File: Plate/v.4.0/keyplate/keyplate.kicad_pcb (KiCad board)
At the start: 2 copper layers, 285.4 x 94.9 mm, 21 parts

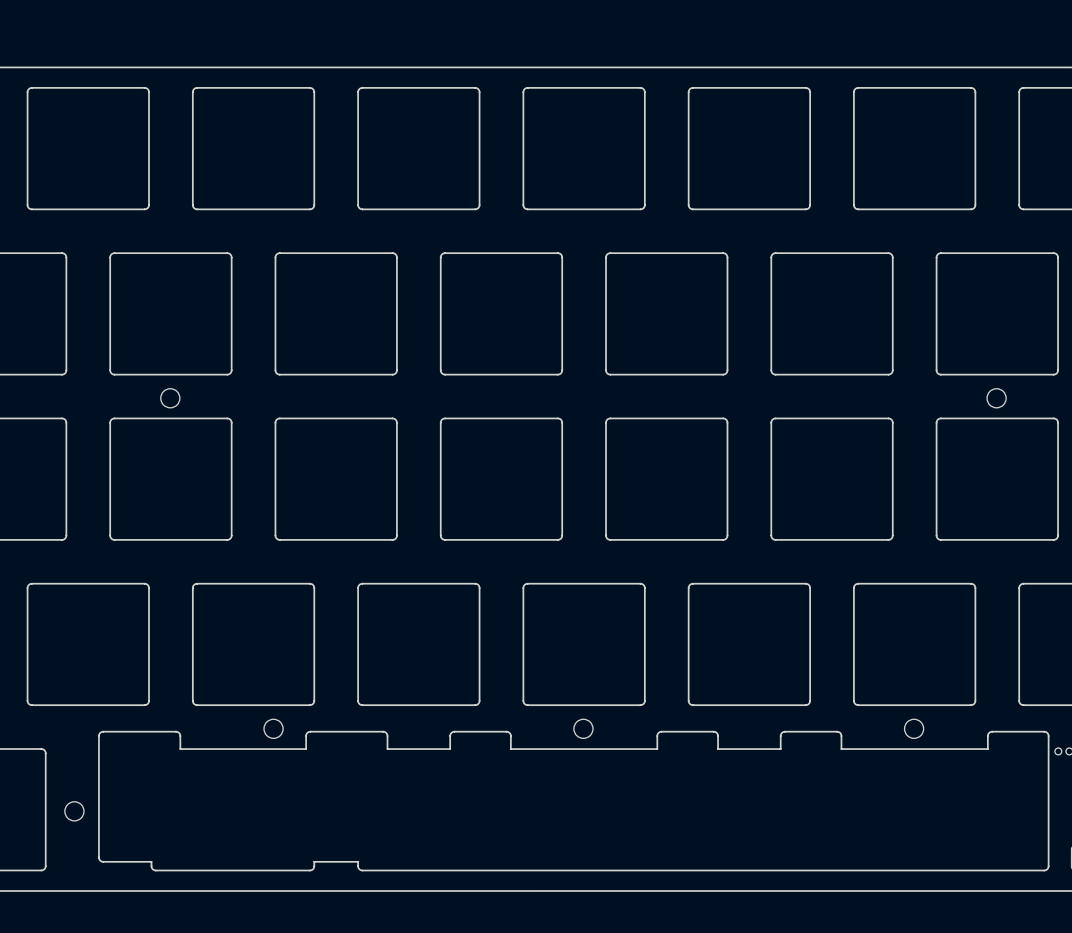
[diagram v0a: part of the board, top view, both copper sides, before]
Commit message: ネジ穴追加など
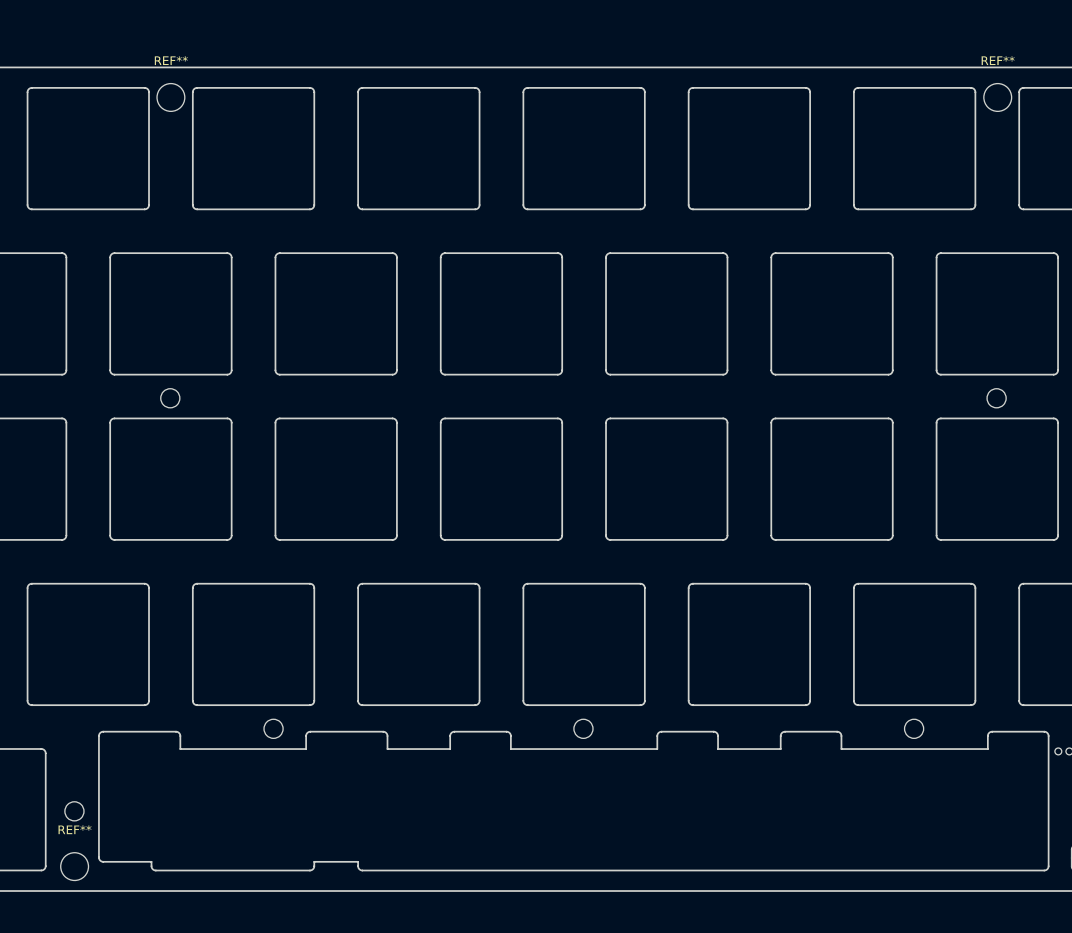
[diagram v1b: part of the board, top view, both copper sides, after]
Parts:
- added REF**: MountingHole_3.2mm_M3, MountingHole:MountingHole_3.2mm_M3, F.Cu at (124.2, 92.5)
- added REF**: MountingHole_3.2mm_M3, MountingHole:MountingHole_3.2mm_M3, F.Cu at (230.7, 3.80)
- added REF**: MountingHole_3.2mm_M3, MountingHole:MountingHole_3.2mm_M3, F.Cu at (135.3, 3.80)
